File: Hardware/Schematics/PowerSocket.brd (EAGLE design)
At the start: 72 x 50 mm, 30 parts, among them IC1 ACS712-LC, T1 BT138-V, T2 BT138-V

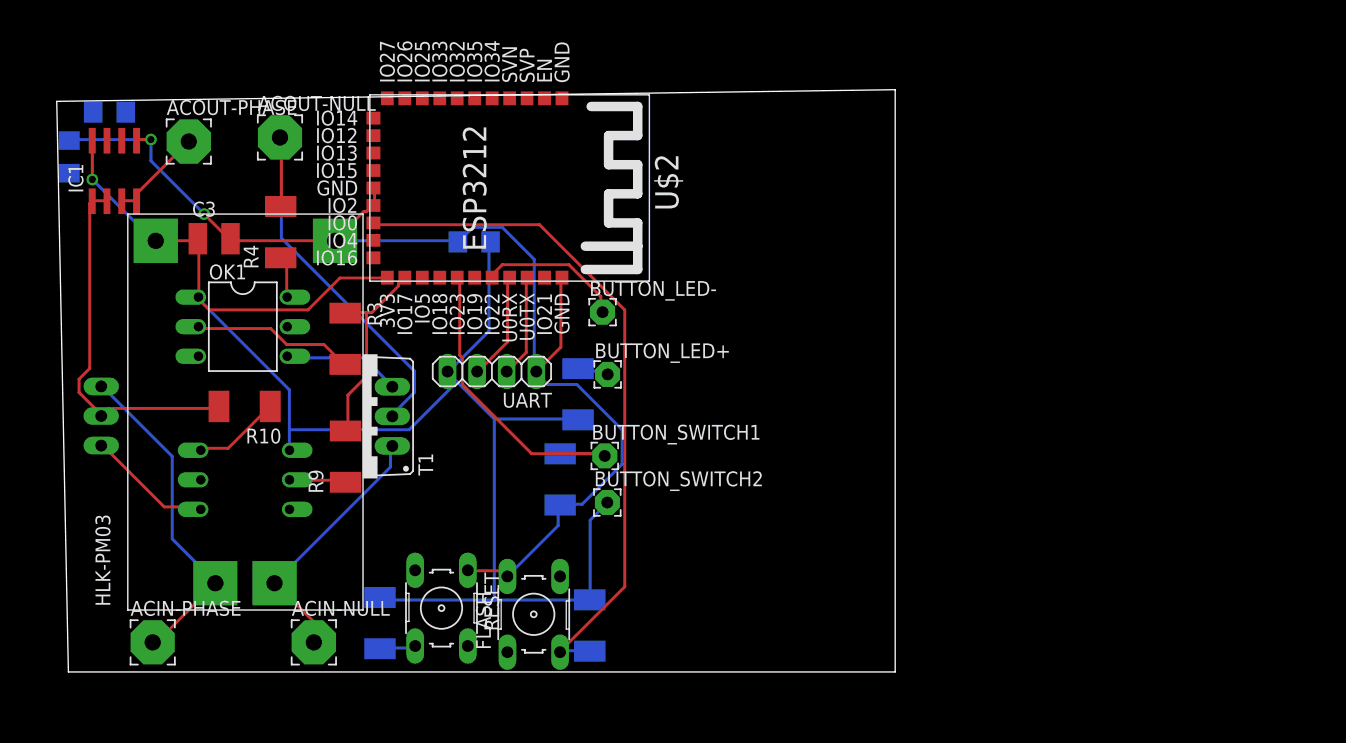
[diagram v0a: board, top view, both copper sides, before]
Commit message: Updated schematic to use for a 3 slot device.
Some routing still remaining.
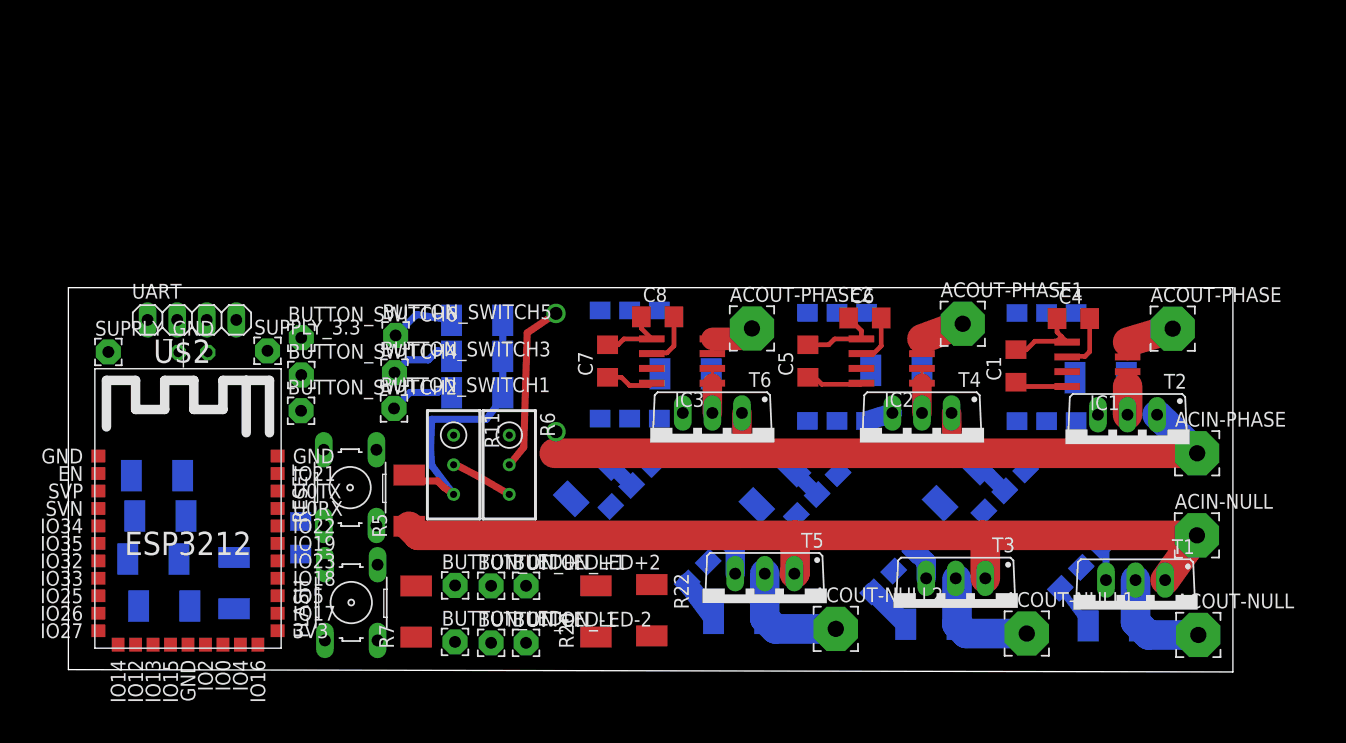
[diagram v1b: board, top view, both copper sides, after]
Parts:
- removed U$1: HLK-PM03, PowerSocket:HLK-PM03
- added ACOUT-NULL1, ACOUT-NULL2, ACOUT-PHASE1, ACOUT-PHASE2: -, wirepad:3,81/1,4
- added BUTTON_LED+1, BUTTON_LED+2, BUTTON_LED-1, BUTTON_LED-2, BUTTON_SWITCH3, BUTTON_SWITCH4, BUTTON_SWITCH5, BUTTON_SWITCH6: -, wirepad:2,15/1,0
- added C5, C7: 100nF, rcl:C1206
- added C6, C8: 470nF, rcl:C1206
- added D1: 1N4004, diode:DO41-10
- added IC2, IC3: ACS712-LC, allegro-2:SOIC8
- added OK3, OK4, OK5, OK6: MOC3041S, optocoupler:DIL6-SMD
- added R11: 10K, rcl:RTRIM3296W
- added R12, R13, R14, R15, R16, R17, R18, R19: 150, eagle-ltspice:R2010
- added R20, R22: 100, eagle-ltspice:R2010
- added R21, R23: 10K, eagle-ltspice:R2010
- added R5: 0, eagle-ltspice:R2010
- added R6: 1M, rcl:RTRIM3296W
- added SUPPLY_3.3: 3.3V, wirepad:2,15/1,0
- added SUPPLY_GND: GND, wirepad:2,15/1,0
- added T3, T4, T5, T6: BT138-V, triac:TO220BV
- C3: device rcl:C1210 -> rcl:C025-024X044
- OK1, OK2: value MOC3041M -> MOC3041S; device optocoupler:DIL06 -> optocoupler:DIL6-SMD
- moved ACIN-PHASE 91.1 mm to (96.9, 18.8)
- moved T2 90.7 mm to (91.0, 19.6), flipped to the top, turned to 180 degrees
- moved ACOUT-NULL 89.7 mm to (97.0, 3.18)
- moved C4 87.3 mm to (86.3, 30.4), flipped to the top, turned to 0 degrees
- moved IC1 86.0 mm to (88.4, 26.4), turned to 90 degrees
- moved ACOUT-PHASE 86.0 mm to (94.8, 29.5)
- moved C1 80.8 mm to (81.4, 26.3), flipped to the top, turned to 90 degrees
- moved R4 79.1 mm to (89.8, 3.96), flipped to the bottom, turned to 180 degrees
- moved ACIN-NULL 76.4 mm to (96.9, 11.7)
- moved R10 73.6 mm to (88.7, 25.3), flipped to the bottom
- moved OK1 70.9 mm to (83.7, 12.3), flipped to the bottom, turned to 135 degrees
- moved OK2 69.5 mm to (84.0, 26.2), turned to 180 degrees
- moved T1 68.4 mm to (91.6, 5.35), turned to 180 degrees
- moved R3 54.1 mm to (76.4, 16.0), flipped to the bottom, turned to 135 degrees
- moved U$2 53.1 mm to (2.27, 2.04), turned to 0 degrees
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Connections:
- removed net N$9 (its old number): ACIN-PHASE.1, T2.T1, U$1.AC1
- new net N$14: ACOUT-NULL1.1, R13.2, T3.T2
- new net N$16: BUTTON_LED+1.1, R20.2
- new net N$24: D1.A, R6.2
- new net N$25: R12.1, R14.2, U$2.IO12
- new net N$26: C6.2, IC2.6
- new net N$27: IC2.7, U$2.IO35
- new net N$28: OK3.2, R12.2
- new net N$29: OK3.6, R13.1
- new net N$3: R11.2, R6.3, U$2.IO26
- new net N$30: OK3.4, T3.G
- new net N$31: BUTTON_LED-1.1, U$2.IO23
- new net N$32: OK4.2, R14.1
- new net N$33: OK4.6, R15.1
- new net N$34: OK4.4, T4.G
- new net N$35: IC2.1, IC2.2, R15.2, T4.T2
- new net N$36: ACOUT-PHASE1.1, IC2.3, IC2.4
- new net N$37: BUTTON_LED+2.1, R22.2
- new net N$38: ACOUT-NULL2.1, R17.2, T5.T2
- new net N$39: BUTTON_SWITCH5.1, R23.2, U$2.IO17
- new net N$40: C8.2, IC3.6
- new net N$41: IC3.7, U$2.IO32
- new net N$42: OK5.2, R16.2
- new net N$43: OK5.6, R17.1
- new net N$44: OK5.4, T5.G
- new net N$45: ACIN-NULL.1, R5.1, T1.T1, T3.T1, T5.T1
- new net N$46: OK6.2, R18.1
- new net N$47: OK6.6, R19.1
- new net N$48: OK6.4, T6.G
- new net N$49: IC3.1, IC3.2, R19.2, T6.T2
- new net N$50: ACOUT-PHASE2.1, IC3.3, IC3.4
- new net N$51: ACIN-PHASE.1, D1.C, T2.T1, T4.T1, T6.T1
- new net N$52: BUTTON_LED-2.1, U$2.IO5
- new net N$54: R16.1, R18.2, U$2.IO14
- net GND: now also C5.2, C6.1, C7.2, C8.1, IC2.5, IC3.5, R11.3, R21.1, R23.1, R5.2, SUPPLY_GND.1; no longer U$1.-VO
- net N$17: now also U$2.IO19; no longer U$2.IO23
- net N$20: now also BUTTON_SWITCH3.1, R21.2, U$2.IO18; no longer ACIN-NULL.1, T1.T1, U$1.AC2
- net N$8: now also U$2.IO13; no longer U$2.IO17
- net VCC: now also BUTTON_SWITCH4.1, BUTTON_SWITCH6.1, C5.1, C7.1, IC2.8, IC3.8, OK3.1, OK4.1, OK5.1, OK6.1, R20.1, R22.1, SUPPLY_3.3.1; no longer U$1.+VO
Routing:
- net VCC: track 138.3 -> 13.6 mm, vias 1 -> 0
- net N$45: track 0.00 -> 79.8 mm
- net N$51: track 0.00 -> 68.9 mm
- net N$7: track 59.0 -> 0.00 mm
- net GND: track 103.4 -> 46.3 mm, vias 2 -> 0
- net N$9 (its old number): track 28.5 -> 0.00 mm
- net N$1: track 35.5 -> 9.45 mm
- net N$23: track 31.5 -> 6.88 mm
- net N$17: track 28.2 -> 5.87 mm
- net N$8: track 17.5 -> 0.00 mm
- net N$20: track 22.5 -> 5.79 mm
- net N$24: track 0.00 -> 14.8 mm
- net N$9: track 12.5 -> 0.00 mm
- net N$22: track 10.8 -> 0.00 mm
- net N$6: track 14.0 -> 3.23 mm
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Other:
- board size 72 x 50 mm -> 100 x 33 mm

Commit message: Added 3d file.
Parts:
- moved R10 182.6 mm to (-90.2, 62.2), flipped to the top, turned to 0 degrees
- moved C4 163.9 mm to (-69.8, 80.0)
- moved C6 161.3 mm to (-85.1, 80.0)
- moved R22 157.8 mm to (-92.7, 72.4), turned to 0 degrees
- moved BUTTON_LED+ 154.8 mm to (-87.6, 104.1)
- moved BUTTON_LED-2 151.0 mm to (-72.4, 104.1)
- moved C5 150.7 mm to (-77.5, 80.0), turned to 0 degrees
- moved C7 148.9 mm to (-92.7, 80.0), turned to 0 degrees
- moved C1 146.2 mm to (-54.6, 80.0), turned to 0 degrees
- moved R20 140.0 mm to (-77.5, 72.4), turned to 0 degrees
- moved BUTTON_LED-1 138.1 mm to (-57.1, 104.1)
- moved R19 131.5 mm to (-69.8, 72.4), flipped to the top, turned to 0 degrees
- moved R21 128.4 mm to (-85.1, 72.4), flipped to the top
- moved BUTTON_LED+2 126.3 mm to (-41.9, 104.1)
- moved BUTTON_SWITCH2 125.4 mm to (-83.8, 92.7)
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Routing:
- net N$51: track 68.9 -> 0.00 mm
- net N$54: track 0.00 -> 56.6 mm
- net VCC: track 13.6 -> 60.1 mm, vias 0 -> 4
- net N$45: track 79.8 -> 33.5 mm
- net GND: track 46.3 -> 0.00 mm
- net N$24: track 14.8 -> 0.00 mm
- net N$43: track 3.79 -> 16.0 mm, vias 0 -> 1
- net N$29: track 3.97 -> 15.5 mm, vias 0 -> 1
- net N$1: track 9.45 -> 0.00 mm
- net N$35: track 7.49 -> 0.00 mm
- net N$49: track 7.23 -> 0.00 mm
- net N$42: track 2.89 -> 10.0 mm
- net N$23: track 6.88 -> 0.00 mm
- net N$17: track 5.87 -> 0.00 mm
- net N$20: track 5.79 -> 0.00 mm
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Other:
- outline, holes or cut-outs redrawn

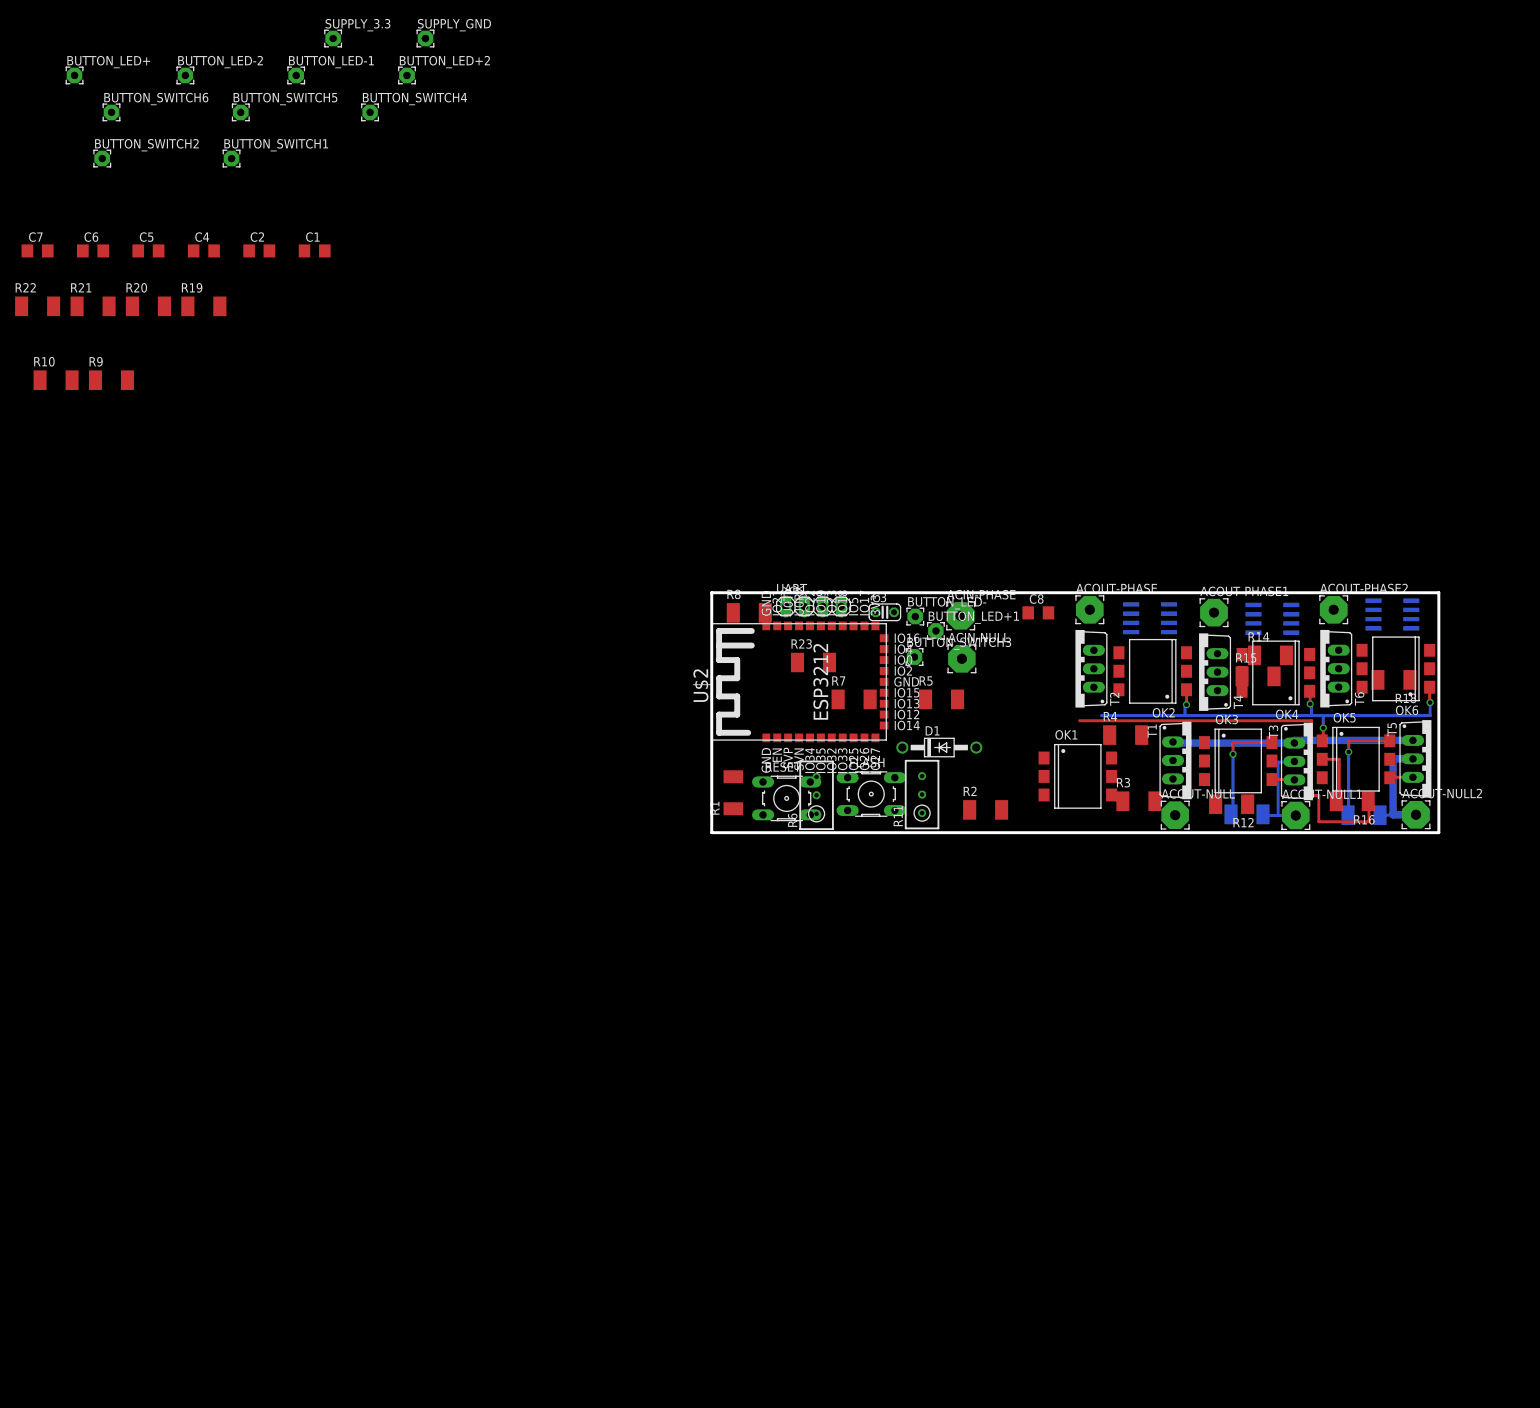
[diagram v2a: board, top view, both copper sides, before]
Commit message: Changed dimension to 50mmx100mm and routed the board
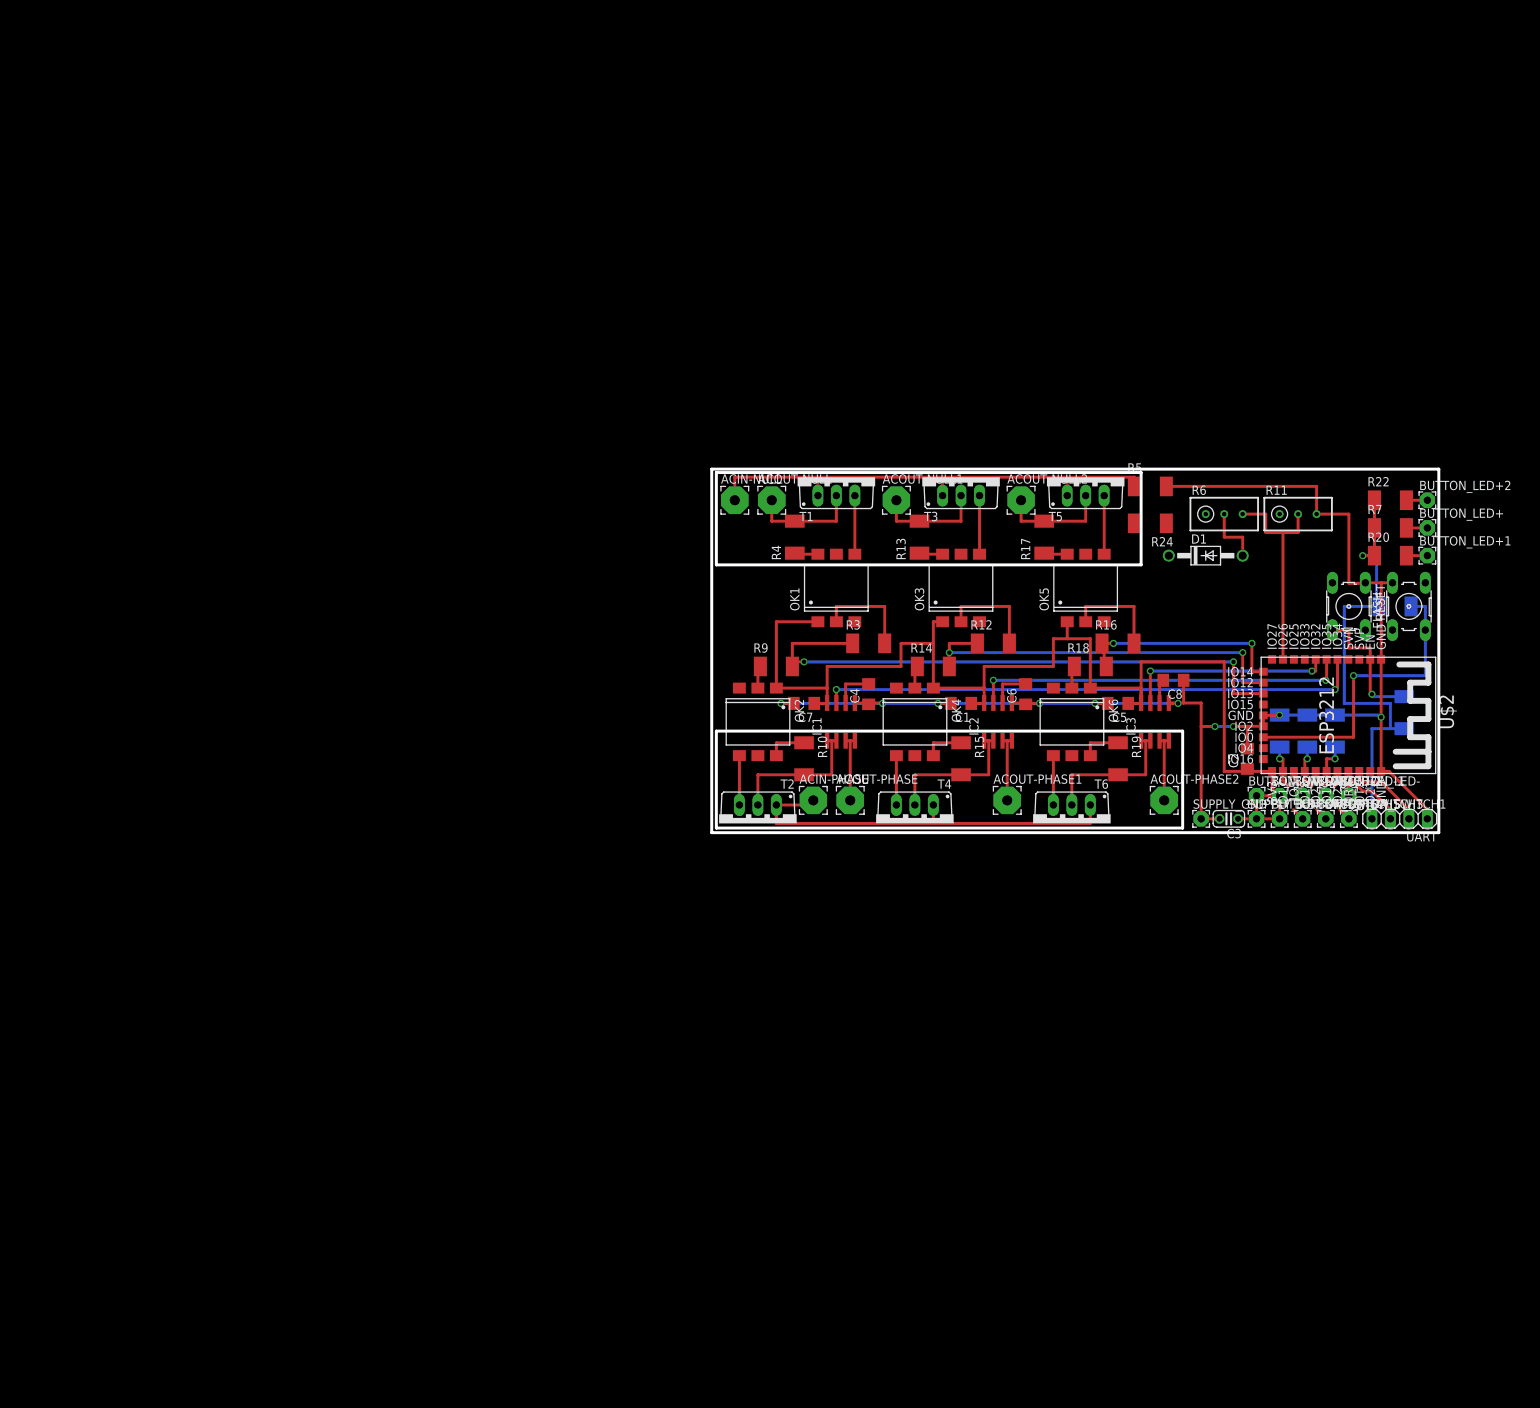
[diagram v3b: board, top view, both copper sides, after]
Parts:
- added R24: 0, eagle-ltspice:R2010
- moved BUTTON_LED+ 196.2 mm to (98.4, 41.9)
- moved R22 188.0 mm to (93.3, 45.7)
- moved BUTTON_SWITCH6 187.7 mm to (78.1, 1.91)
- moved BUTTON_SWITCH2 184.1 mm to (78.1, 5.08)
- moved BUTTON_LED-2 182.8 mm to (81.3, 5.08)
- moved BUTTON_SWITCH1 178.5 mm to (87.6, 1.91)
- moved R21 176.9 mm to (81.9, 14.0), flipped to the bottom, turned to 270 degrees
- moved BUTTON_SWITCH5 175.4 mm to (81.3, 1.91)
- moved R20 174.2 mm to (93.3, 38.1)
- moved BUTTON_LED-1 172.8 mm to (84.5, 5.08)
- moved SUPPLY_3.3 166.3 mm to (74.9, 1.91)
- moved BUTTON_SWITCH4 153.9 mm to (74.9, 5.08)
- moved C2 152.8 mm to (73.7, 10.2), turned to 90 degrees
- moved BUTTON_LED+2 152.0 mm to (98.4, 45.7)
- moved SUPPLY_GND 151.3 mm to (67.3, 1.91)
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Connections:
- new net N$53: D1.C, R24.1
- net N$51: now also R24.2; no longer D1.C
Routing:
- net GND: track 0.00 -> 205.4 mm, vias 0 -> 10
- net VCC: track 60.1 -> 231.4 mm, vias 4 -> 1
- net N$8: track 0.00 -> 80.6 mm, vias 0 -> 2
- net N$12: track 0.00 -> 74.9 mm, vias 0 -> 2
- net N$51: track 0.00 -> 56.5 mm
- net N$25: track 0.00 -> 54.3 mm, vias 0 -> 2
- net N$27: track 0.00 -> 51.8 mm, vias 0 -> 2
- net N$7: track 0.00 -> 42.2 mm, vias 0 -> 1
- net N$45: track 33.5 -> 67.0 mm
- net N$3: track 0.00 -> 30.1 mm
- net N$41: track 0.00 -> 28.7 mm, vias 0 -> 2
- net N$54: track 56.6 -> 29.9 mm, vias 0 -> 2
- net N$35: track 0.00 -> 20.9 mm
- net N$23: track 0.00 -> 20.3 mm
- net N$49: track 0.00 -> 20.3 mm
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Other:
- board size 100 x 33 mm -> 100 x 50 mm
